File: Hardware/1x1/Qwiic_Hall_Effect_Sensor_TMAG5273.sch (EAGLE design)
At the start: 32 parts, among them J1 QWIIC_RIGHT_ANGLE, J2 QWIIC_RIGHT_ANGLE, Q1 20V/4.2A/52mΩ/1.4W, U1 TMAG5273

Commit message: Ready for review
Updates from ENG Checklist - Small tweaks added  - updated ordering of PTH headers for SDA and SCL, fixed final errors on design
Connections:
- net GPIO: now also J3.5; no longer J3.3
- net SCL: now also J3.4; no longer J3.5
- net SDA: now also J3.3; no longer J3.4
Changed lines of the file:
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@@
 <grid distance="0.1" unitdist="inch" unit="inch" style="lines" multiple="1" display="no" altdistance="0.01" altunitdist="inch" altunit="inch"/>
 <layers>
-<layer number="1" name="Top" color="4" fill="1" visible="yes" active="no"/>
-<layer number="2" name="Route2" color="16" fill="1" visible="yes" active="no"/>
-<layer number="15" name="Route15" color="23" fill="1" visible="yes" active="no"/>
-<layer number="16" name="Bottom" color="1" fill="1" visible="yes" active="no"/>
-<layer number="17" name="Pads" color="2" fill="1" visible="yes" active="no"/>
-<layer number="18" name="Vias" color="2" fill="1" visible="yes" active="no"/>
-<layer number="19" name="Unrouted" color="6" fill="1" visible="yes" active="no"/>
-<layer number="20" name="Dimension" color="24" fill="1" visible="yes" active="no"/>
-<layer number="21" name="tPlace" color="16" fill="1" visible="yes" active="no"/>
-<layer number="22" name="bPlace" color="14" fill="1" visible="yes" active="no"/>
-<layer number="23" name="tOrigins" color="15" fill="1" visible="yes" active="no"/>
-<layer number="24" name="bOrigins" color="15" fill="1" visible="yes" active="no"/>
-<layer number="25" name="tNames" color="7" fill="1" visible="yes" active="no"/>
-<layer number="26" name="bNames" color="7" fill="1" visible="yes" active="no"/>
-<layer number="27" name="tValues" color="7" fill="1" visible="yes" active="no"/>
-<layer number="28" name="bValues" color="7" fill="1" visible="yes" active="no"/>
+<layer number="1" name="Top" color="4" fill="1" visible="no" active="no"/>
+<layer number="2" name="Route2" color="16" fill="1" visible="no" active="no"/>
+<layer number="15" name="Route15" color="23" fill="1" visible="no" active="no"/>
+<layer number="16" name="Bottom" color="1" fill="1" visible="no" active="no"/>
+<layer number="17" name="Pads" color="2" fill="1" visible="no" active="no"/>
+<layer number="18" name="Vias" color="2" fill="1" visible="no" active="no"/>
+<layer number="19" name="Unrouted" color="6" fill="1" visible="no" active="no"/>
+<layer number="20" name="Dimension" color="24" fill="1" visible="no" active="no"/>
+<layer number="21" name="tPlace" color="16" fill="1" visible="no" active="no"/>
+<layer number="22" name="bPlace" color="14" fill="1" visible="no" active="no"/>
+<layer number="23" name="tOrigins" color="15" fill="1" visible="no" active="no"/>
+<layer number="24" name="bOrigins" color="15" fill="1" visible="no" active="no"/>
+<layer number="25" name="tNames" color="7" fill="1" visible="no" active="no"/>
+<layer number="26" name="bNames" color="7" fill="1" visible="no" active="no"/>
+<layer number="27" name="tValues" color="7" fill="1" visible="no" active="no"/>
+<layer number="28" name="bValues" color="7" fill="1" visible="no" active="no"/>
 <layer number="29" name="tStop" color="7" fill="3" visible="no" active="no"/>
 <layer number="30" name="bStop" color="7" fill="6" visible="no" active="no"/>
@@
 <layer number="35" name="tGlue" color="7" fill="4" visible="no" active="no"/>
 <layer number="36" name="bGlue" color="7" fill="5" visible="no" active="no"/>
-<layer number="37" name="tTest" color="7" fill="1" visible="yes" active="no"/>
-<layer number="38" name="bTest" color="7" fill="1" visible="yes" active="no"/>
+<layer number="37" name="tTest" color="7" fill="1" visible="no" active="no"/>
+<layer number="38" name="bTest" color="7" fill="1" visible="no" active="no"/>
 <layer number="39" name="tKeepout" color="4" fill="11" visible="no" active="no"/>
 <layer number="40" name="bKeepout" color="1" fill="11" visible="no" active="no"/>
@@
 <layer number="44" name="Drills" color="7" fill="1" visible="no" active="no"/>
 <layer number="45" name="Holes" color="7" fill="1" visible="no" active="no"/>
-<layer number="46" name="Milling" color="3" fill="1" visible="yes" active="no"/>
-<layer number="47" name="Measures" color="7" fill="1" visible="yes" active="no"/>
-<layer number="48" name="Document" color="7" fill="1" visible="yes" active="no"/>
-<layer number="49" name="Reference" color="7" fill="1" visible="yes" active="no"/>
-<layer number="50" name="dxf" color="7" fill="1" visible="yes" active="no"/>
-<layer number="51" name="tDocu" color="6" fill="1" visible="yes" active="no"/>
-<layer number="52" name="bDocu" color="7" fill="1" visible="yes" active="no"/>
-<layer number="53" name="tGND_GNDA" color="7" fill="9" visible="yes" active="no"/>
-<layer number="54" name="bGND_GNDA" color="1" fill="9" visible="yes" active="no"/>
-<layer number="56" name="wert" color="7" fill="1" visible="yes" active="no"/>
-<layer number="57" name="tCAD" color="7" fill="1" visible="yes" active="no"/>
-<layer number="58" name="bCAD" color="7" fill="1" visible="yes" active="no"/>
-<layer number="59" name="tCarbon" color="7" fill="1" visible="yes" active="no"/>
-<layer number="60" name="bCarbon" color="7" fill="1" visible="yes" active="no"/>
+<layer number="46" name="Milling" color="3" fill="1" visible="no" active="no"/>
+<layer number="47" name="Measures" color="7" fill="1" visible="no" active="no"/>
+<layer number="48" name="Document" color="7" fill="1" visible="no" active="no"/>
+<layer number="49" name="Reference" color="7" fill="1" visible="no" active="no"/>
+<layer number="50" name="dxf" color="7" fill="1" visible="no" active="no"/>
+<layer number="51" name="tDocu" color="6" fill="1" visible="no" active="no"/>
+<layer number="52" name="bDocu" color="7" fill="1" visible="no" active="no"/>
+<layer number="53" name="tGND_GNDA" color="7" fill="9" visible="no" active="no"/>
+<layer number="54" name="bGND_GNDA" color="1" fill="9" visible="no" active="no"/>
+<layer number="56" name="wert" color="7" fill="1" visible="no" active="no"/>
+<layer number="57" name="tCAD" color="7" fill="1" visible="no" active="no"/>
+<layer number="58" name="bCAD" color="7" fill="1" visible="no" active="no"/>
+<layer number="59" name="tCarbon" color="7" fill="1" visible="no" active="no"/>
+<layer number="60" name="bCarbon" color="7" fill="1" visible="no" active="no"/>
 <layer number="88" name="SimResults" color="9" fill="1" visible="yes" active="yes"/>
 <layer number="89" name="SimProbes" color="9" fill="1" visible="yes" active="yes"/>
@@
 </segment>
 <segment>
-<wire x1="30.48" y1="73.66" x2="35.56" y2="73.66" width="0.1524" layer="91"/>
-<label x="35.56" y="73.66" size="1.27" layer="95" font="vector" xref="yes"/>
-<pinref part="J3" gate="J1" pin="5"/>
-</segment>
-<segment>
 <pinref part="R5" gate="G$1" pin="1"/>
 <wire x1="233.68" y1="129.54" x2="233.68" y2="127" width="0.1524" layer="91"/>
@@
 <label x="129.54" y="76.2" size="1.27" layer="95" font="vector" xref="yes"/>
 </segment>
+<segment>
+<wire x1="30.48" y1="71.12" x2="35.56" y2="71.12" width="0.1524" layer="91"/>
+<label x="35.56" y="71.12" size="1.27" layer="95" font="vector" xref="yes"/>
+<pinref part="J3" gate="J1" pin="4"/>
+</segment>
 </net>
 <net name="SDA" class="0">
@@
 <wire x1="147.32" y1="144.78" x2="144.78" y2="144.78" width="0.1524" layer="91"/>
 <label x="147.32" y="144.78" size="1.27" layer="95" font="vector" xref="yes"/>
-</segment>
-<segment>
-<wire x1="30.48" y1="71.12" x2="35.56" y2="71.12" width="0.1524" layer="91"/>
-<label x="35.56" y="71.12" size="1.27" layer="95" font="vector" xref="yes"/>
-<pinref part="J3" gate="J1" pin="4"/>
 </segment>
 <segment>
@@
 <wire x1="124.46" y1="73.66" x2="129.54" y2="73.66" width="0.1524" layer="91"/>
 <label x="129.54" y="73.66" size="1.27" layer="95" font="vector" xref="yes"/>
+</segment>
+<segment>
+<wire x1="30.48" y1="68.58" x2="35.56" y2="68.58" width="0.1524" layer="91"/>
+<label x="35.56" y="68.58" size="1.27" layer="95" font="vector" xref="yes"/>
+<pinref part="J3" gate="J1" pin="3"/>
 </segment>
 </net>
@@
 </segment>
 <segment>
-<pinref part="J3" gate="J1" pin="3"/>
-<wire x1="30.48" y1="68.58" x2="35.56" y2="68.58" width="0.1524" layer="91"/>
-<label x="35.56" y="68.58" size="1.27" layer="95" font="vector" xref="yes"/>
-</segment>
-</net>
+<wire x1="30.48" y1="73.66" x2="35.56" y2="73.66" width="0.1524" layer="91"/>
+<label x="35.56" y="73.66" size="1.27" layer="95" font="vector" xref="yes"/>
+<pinref part="J3" gate="J1" pin="5"/>
+</segment>
+</net>

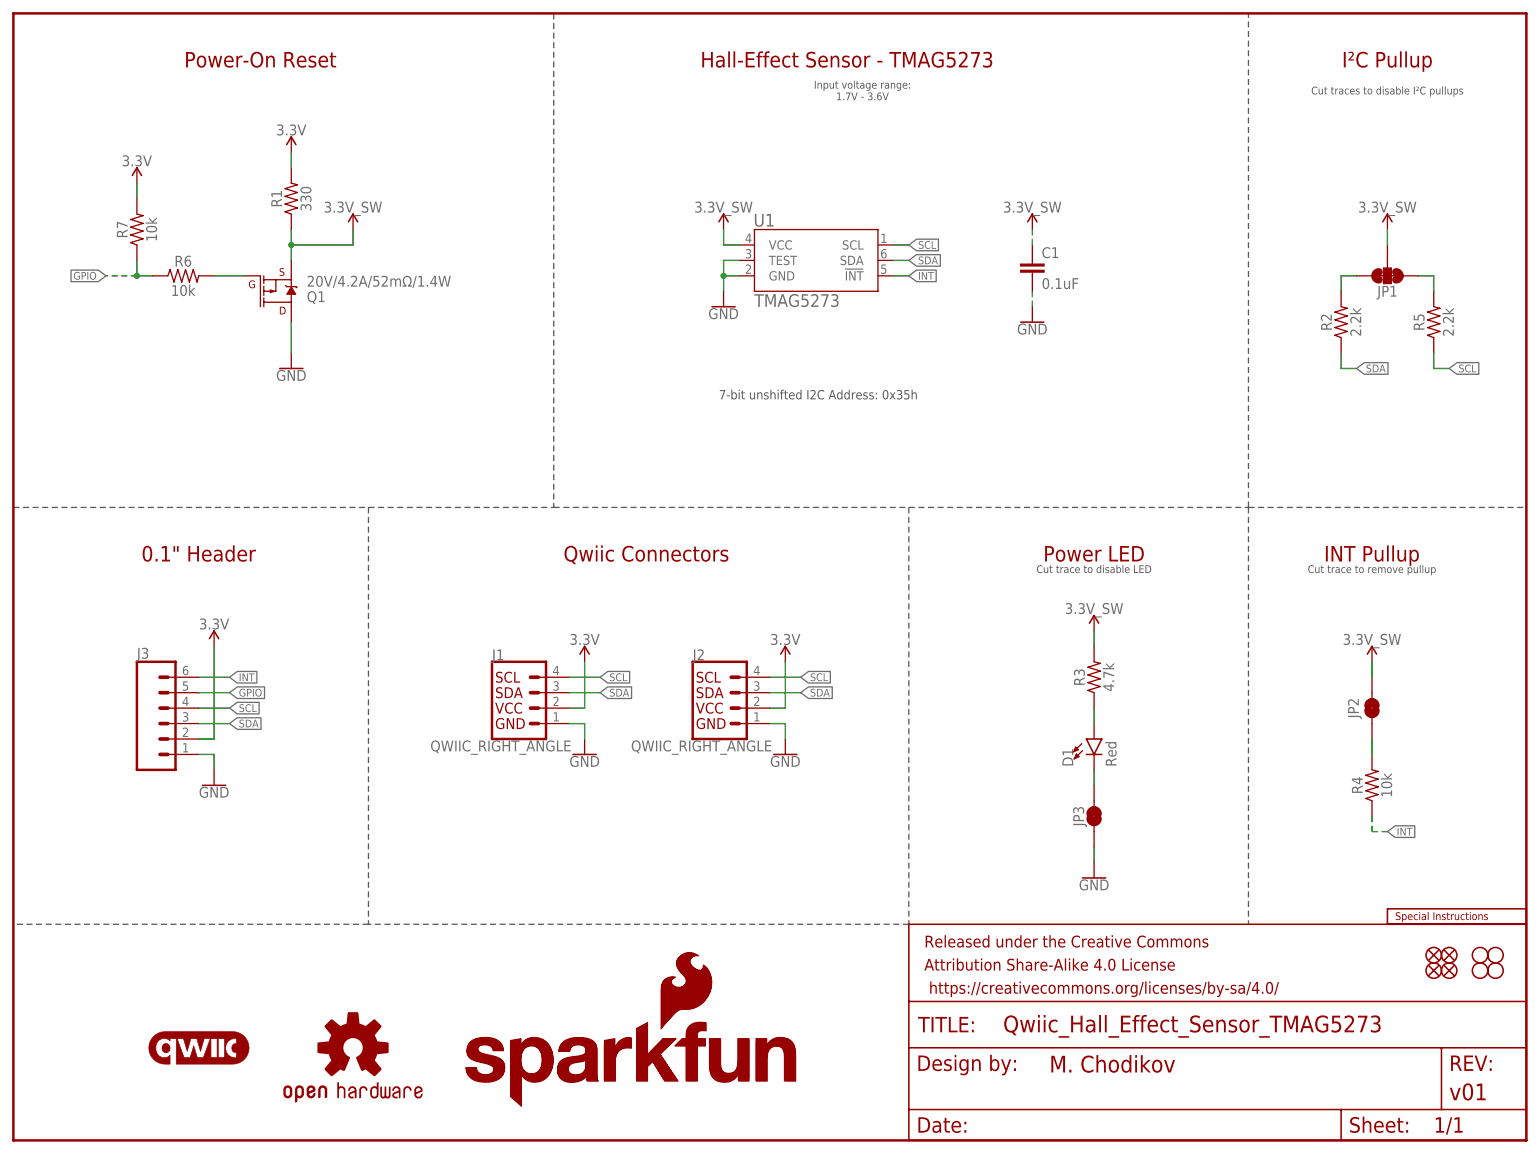
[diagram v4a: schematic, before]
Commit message: Design Review Changes
Adjusted schematic to have the correct power-on reset circuit, along with the change in the layout. The GPIO net was relabled to RESET to match the layout of the board/labeling. Adjusted some labeling in the schematic.
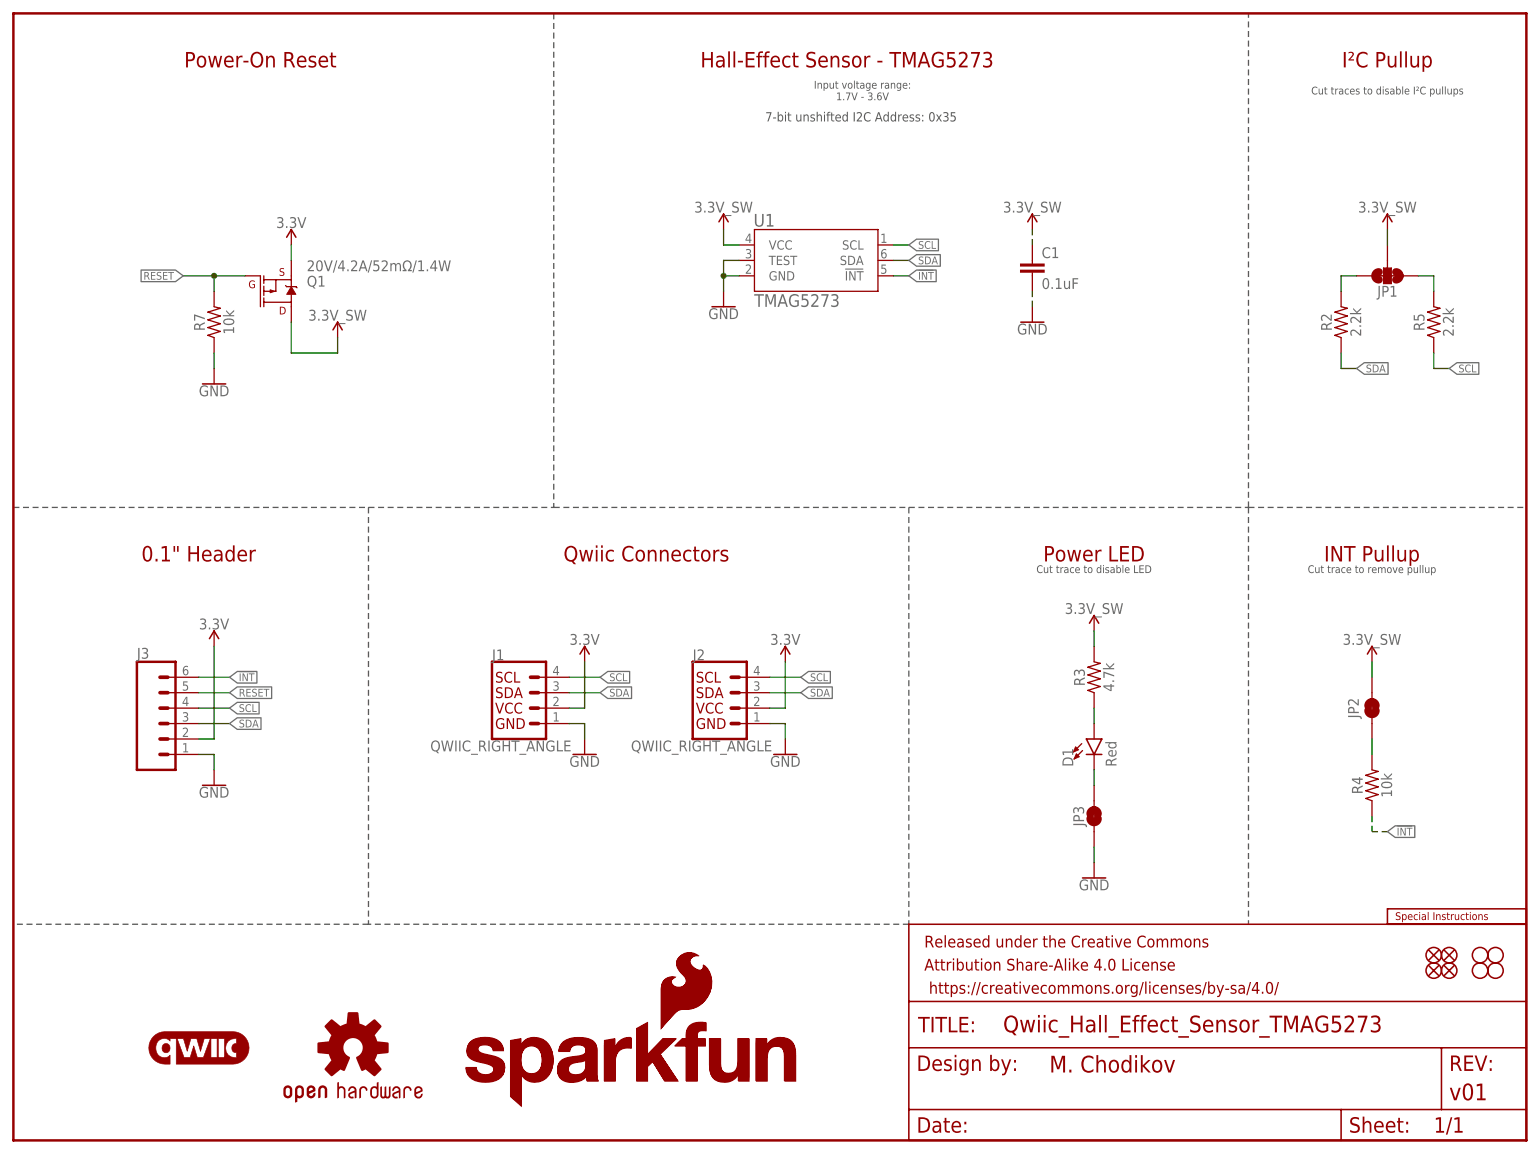
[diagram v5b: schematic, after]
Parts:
- removed R1: 330, SparkFun-Resistors:330OHM-0603-1/10W-1%
- removed R6: 10k, SparkFun-Resistors:10KOHM-0603-1/10W-1%
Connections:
- net INT renamed !INT
- removed net GPIO: J3.5, R6.1, R7.1
- removed net N$7: Q1.G, R6.2
- new net RESET: J3.5, Q1.G, R7.2
- net 3.3V: now also Q1.S; no longer R1.2, R7.2
- net 3.3V_SW: now also Q1.D; no longer Q1.S, R1.1
- net GND: now also R7.1; no longer Q1.D
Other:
- note added: "7-bit unshifted I2C Address: 0x35"
- note removed: "7-bit unshifted I2C Address: 0x35h"
- moved on the sheet: R7

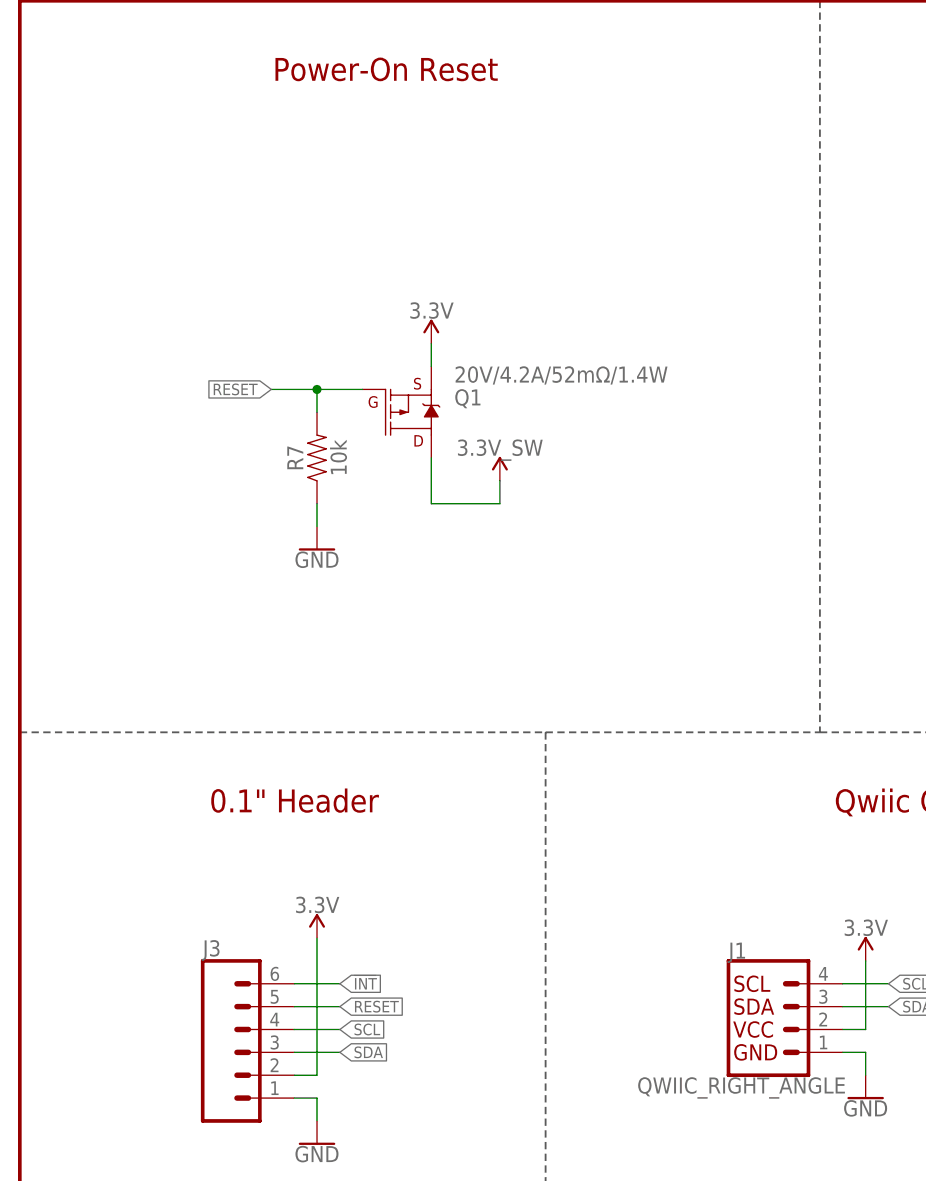
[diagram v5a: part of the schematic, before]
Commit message: Adjusted from design review
Added truth tables, changed RESET to Disable, adjusted magnetic axis to be centered to the middle of the board, added push button for 1x1 reset option
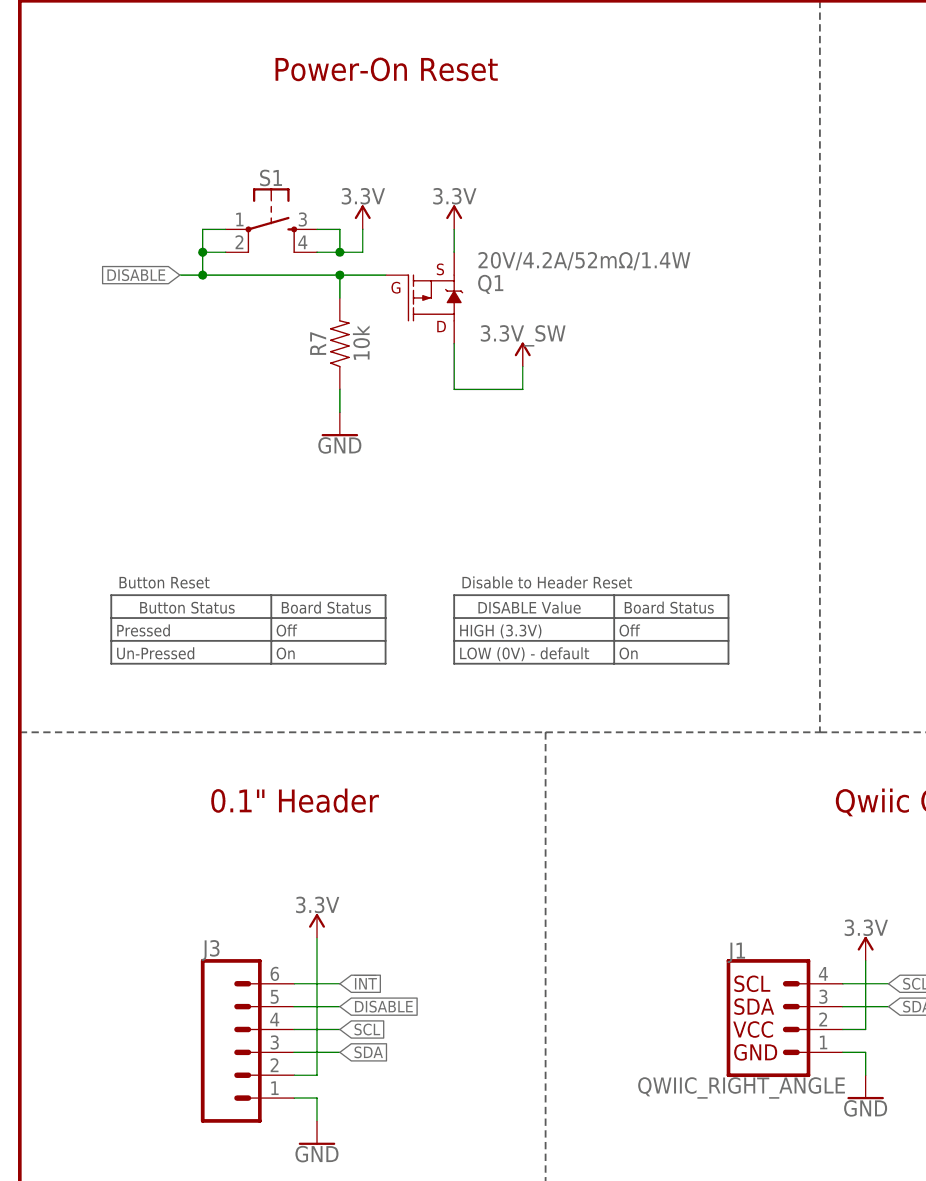
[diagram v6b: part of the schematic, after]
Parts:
- added S1: (no value), SparkFun-Switches:MOMENTARY-SWITCH-SPST-2-SMD-4.6X2.8MM
- LOGO3: value QWIIC_LOGO_CONNECTOR -> QWIIC_LOGO_4MM; device SparkFun-Aesthetics:QWIIC_LOGO_CONNECTOR -> SparkFun-Aesthetics:QWIIC_LOGO_4MM
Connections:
- removed net RESET: J3.5, Q1.G, R7.2
- new net DISABLE: J3.5, Q1.G, R7.2, S1.1, S1.2
- net 3.3V: now also S1.3, S1.4
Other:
- note added: "Board Status"
- note added: "Button Reset"
- note added: "Button Status"
- note added: "DISABLE Value"
- note added: "Disable to Header Reset"
- note added: "HIGH (3.3V)"
- note added: "LOW (0V) - default"
- note added: "Off"
- note added: "On"
- note added: "Pressed"
- note added: "Un-Pressed"
- moved on the sheet: Q1, R7
